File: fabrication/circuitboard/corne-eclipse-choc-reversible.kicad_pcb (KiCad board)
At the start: 4 copper layers, 150.6 x 105.7 mm, 91 parts, among them J2 OLED, SW1 SW_Choc_v1v2_HS, SW10 SW_Choc_v1v2_HS, SW11 SW_Choc_v1v2_HS, SW12 SW_Choc_v1v2_HS, SW13 SW_Choc_v1v2_HS, SW14 SW_Choc_v1v2_HS, SW15 SW_Choc_v1v2_HS, SW16 SW_Choc_v1v2_HS, SW17 SW_Choc_v1v2_HS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

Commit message: fix(pcb): rename nice!view nets to match SPI pinout (SDA→DISP_MOSI, SCL→DISP_SCK, data→DISP_CS)
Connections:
- net SCL renamed DISP_SCK
- net SDA renamed DISP_MOSI
- net data renamed DISP_CS

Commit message: fix(pcb): rename nets to match canonical nice!nano pinout (LED_CHAIN, VIEW_*, ROW1-4, COL0-5, ENC_A/B, BAT+)
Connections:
- net BAT1+ renamed BAT+
- net DISP_CS renamed VIEW_CS
- net DISP_MOSI renamed VIEW_MOSI
- net DISP_SCK renamed VIEW_SCK
- net LED renamed LED_CHAIN
- net Net-(U1-Pad11) renamed ENC_A
- net Net-(U1-Pad12) renamed ENC_B
- net col0 renamed COL0
- net col1 renamed COL1
- net col2 renamed COL2
- net col3 renamed COL3
- net col4 renamed COL4
- net col5 renamed COL5
- net reset renamed RESET
- net row0 renamed ROW1
- net row1 renamed ROW2
- net row2 renamed ROW3
- net row3 renamed ROW4

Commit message: fix(pcb): rename Net-(U1-Pad24) to RAW (post-switch/diode rail to MCU)
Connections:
- net Net-(U1-Pad24) renamed RAW
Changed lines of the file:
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@@
 			(size 0.2 0.2)
 			(layers "F.Cu" "F.Mask")
-			(net "Net-(U1-Pad24)")
+			(net "RAW")
 		)
 		(pad "24" smd custom
@@
 			(size 1.6 1.6)
 			(layers "F.Cu" "F.Mask")
-			(net "Net-(U1-Pad24)")
+			(net "RAW")
 			(thermal_bridge_angle 90)
 			(options
@@
 			(size 2 2)
 			(layers "F.Cu" "F.Mask")
-			(net "Net-(U1-Pad24)")
+			(net "RAW")
 			(zone_connect 0)
 		)
@@
 			(size 0.8 0.8)
 			(layers "F.Cu")
-			(net "Net-(U1-Pad24)")
+			(net "RAW")
 			(options
 				(clearance outline)
@@
 			(size 0.8 0.8)
 			(layers "B.Cu")
-			(net "Net-(U1-Pad24)")
+			(net "RAW")
 			(options
 				(clearance outline)
@@
 			(layers "*.Cu")
 			(remove_unused_layers no)
-			(net "Net-(U1-Pad24)")
+			(net "RAW")
 		)
 		(pad "24" smd custom
@@
 			(size 1.6 1.6)
 			(layers "B.Cu" "B.Mask")
-			(net "Net-(U1-Pad24)")
+			(net "RAW")
 			(thermal_bridge_angle 90)
 			(options
@@
 			(size 2 2)
 			(layers "B.Cu" "B.Mask")
-			(net "Net-(U1-Pad24)")
+			(net "RAW")
 			(zone_connect 0)
 		)
@@
 			(size 0.2 0.2)
 			(layers "B.Cu" "B.Mask")
-			(net "Net-(U1-Pad24)")
+			(net "RAW")
 		)
 		(embedded_fonts no)
@@
 			(layers "*.Cu" "*.Mask")
 			(remove_unused_layers no)
-			(net "Net-(U1-Pad24)")
+			(net "RAW")
 		)
 		(pad "2" thru_hole oval
@@
 		(width 0.2)
 		(layer "F.Cu")
-		(net "Net-(U1-Pad24)")
+		(net "RAW")
 	)
 	(segment
@@
 		(width 0.2)
 		(layer "F.Cu")
-		(net "Net-(U1-Pad24)")
+		(net "RAW")
 	)
 	(segment
@@
 		(width 0.2)
 		(layer "F.Cu")
-		(net "Net-(U1-Pad24)")
+		(net "RAW")
 	)
 	(segment
@@
 		(width 0.2)
 		(layer "F.Cu")
-		(net "Net-(U1-Pad24)")
+		(net "RAW")
 	)
 	(segment
@@
 		(width 0.2)
 		(layer "F.Cu")
-		(net "Net-(U1-Pad24)")
+		(net "RAW")
 	)
 	(segment
@@
 		(width 0.2)
 		(layer "F.Cu")
-		(net "Net-(U1-Pad24)")
+		(net "RAW")
 	)
 	(segment

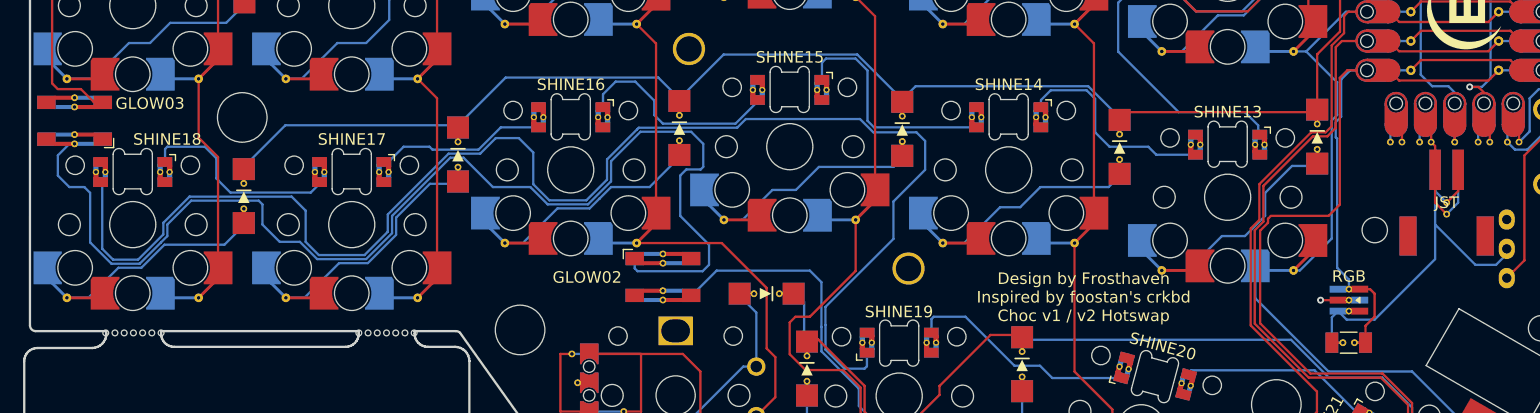
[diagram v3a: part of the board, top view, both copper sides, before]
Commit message: fix(pcb): correct MOSFET and GLOW03 net assignments
Two unrelated net-swap bugs in the choc-reversible PCB, both fixed by
swapping net metadata and re-routing traces:

1. SOT-23-reversible footprint (RGBMOS) had Pad 1 and Pad 2 net
   assignments inverted vs. the standard AO3401A pinout, so Gate ended
   up on BAT+ and Source on EXT_PWR (P-FET never switched). Swapped
   Pad 1 → BAT+, Pad 2 → EXT_PWR.

2. GLOW03's data-line nets were swapped on Pad 2 (DOUT) and Pad 4
   (DIN), so the LED received no data and its DOUT shorted to GLOW02's
   DOUT. Swapped to chain in/out correctly.
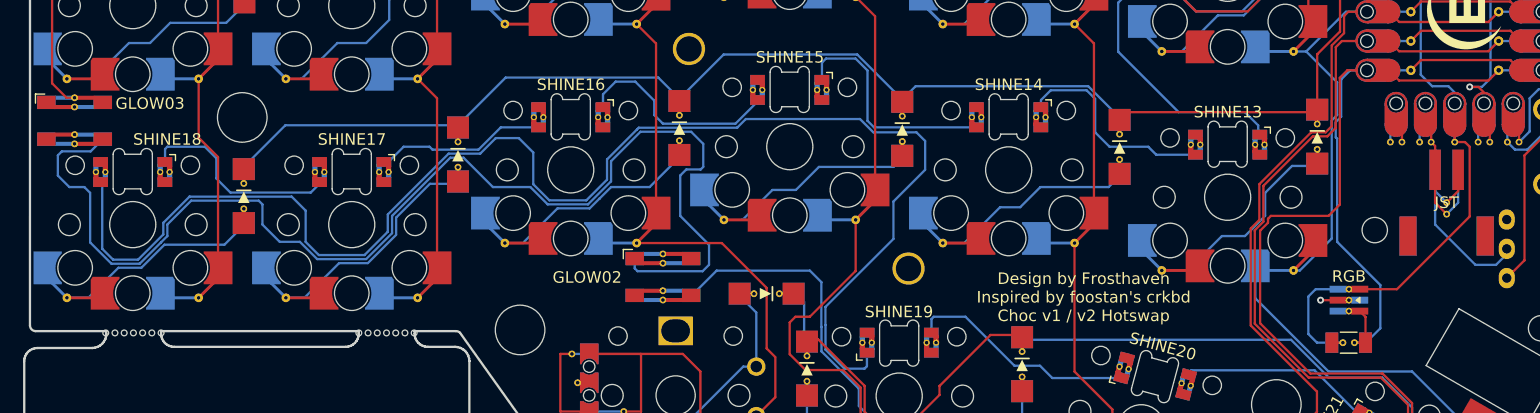
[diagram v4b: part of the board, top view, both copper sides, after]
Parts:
- turned GLOW03 to 0 degrees
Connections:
- GLOW03 pad 2: led24-led25 -> led25-led26
- GLOW03 pad 4: led25-led26 -> led24-led25
- R1 pad 2: BAT+ -> VCC
- RGBMOS pad 1: EXT_PWR -> VCC
- RGBMOS pad 2: BAT+ -> EXT_PWR
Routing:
- net VCC: track 27.5 -> 55.7 mm
- net BAT+: track 36.7 -> 19.8 mm
- net EXT_PWR: track 26.5 -> 29.8 mm
- net led24-led25: track 102.3 -> 105.0 mm
- net led25-led26: track 47.5 -> 45.0 mm
